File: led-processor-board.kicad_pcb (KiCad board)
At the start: 2 copper layers, 100 x 89.5 mm, 127 parts, among them J1 USB-C, J2 SPARE, J3 SWD, J4 12V IN, J5 OUT1, J6 OUT2, J7 OUT3, J8 OUT4, SW1 434133025816, SW2 434133025816, U1 RP2350B, U2 NCP1117ST33T3G, U3 W25Q128JVSIQ, U4 APS6404L-3SQR-SN, U5 RM2, U6 DS3231SN, U7 TPS54202H, X1 12MHz

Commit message: Move the PSRAM to the top side for one-sided JLCPCB assembly
U4 (APS6404L) and its C22, R11 and R13 were under the flash on the bottom,
as on Pi's board. They now sit on top just left of the flash, with the
QSPI branches run from Pi's vias under U3, so every part is on the top.
DRC: nothing unconnected, no copper errors.

Co-Authored-By: Claude Opus 5.5 (1M context) <noreply@anthropic.com>
Claude-Session: https://claude.ai/code/session_01CYnkeL97vxsPSCyXSKGro9
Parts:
- C22, R11, R13, U4: moved to F.Cu
- moved R11 20.5 mm to (73.0, 77.4), turned to 0 degrees
- moved R13 19.6 mm to (73.0, 75.2)
- moved U4 16.3 mm to (79.5, 78.0), turned to 0 degrees
- moved C22 10.2 mm to (83.0, 73.6), turned to 0 degrees
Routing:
- net /GPIO47_ADC7: track 36.1 -> 60.2 mm, vias 1 -> 2
- net /QSPI_SD3: track 17.0 -> 40.0 mm, vias 1 -> 3
- net /QSPI_SD2: track 18.3 -> 38.4 mm, vias 1 -> 2
- net +3V3: track 235.0 -> 249.5 mm, vias 14 -> 15
- net /QSPI_SD0: track 13.8 -> 26.9 mm, vias 1 -> 2
- net /QSPI_SCLK: track 15.5 -> 28.3 mm, vias 1 -> 2
- net /QSPI_SD1: track 23.4 -> 35.9 mm, vias 1 -> 2
- net /PSRAM_CS: track 7.27 -> 6.23 mm
- net GND: track 58.3 -> 59.3 mm, vias 143 -> 141

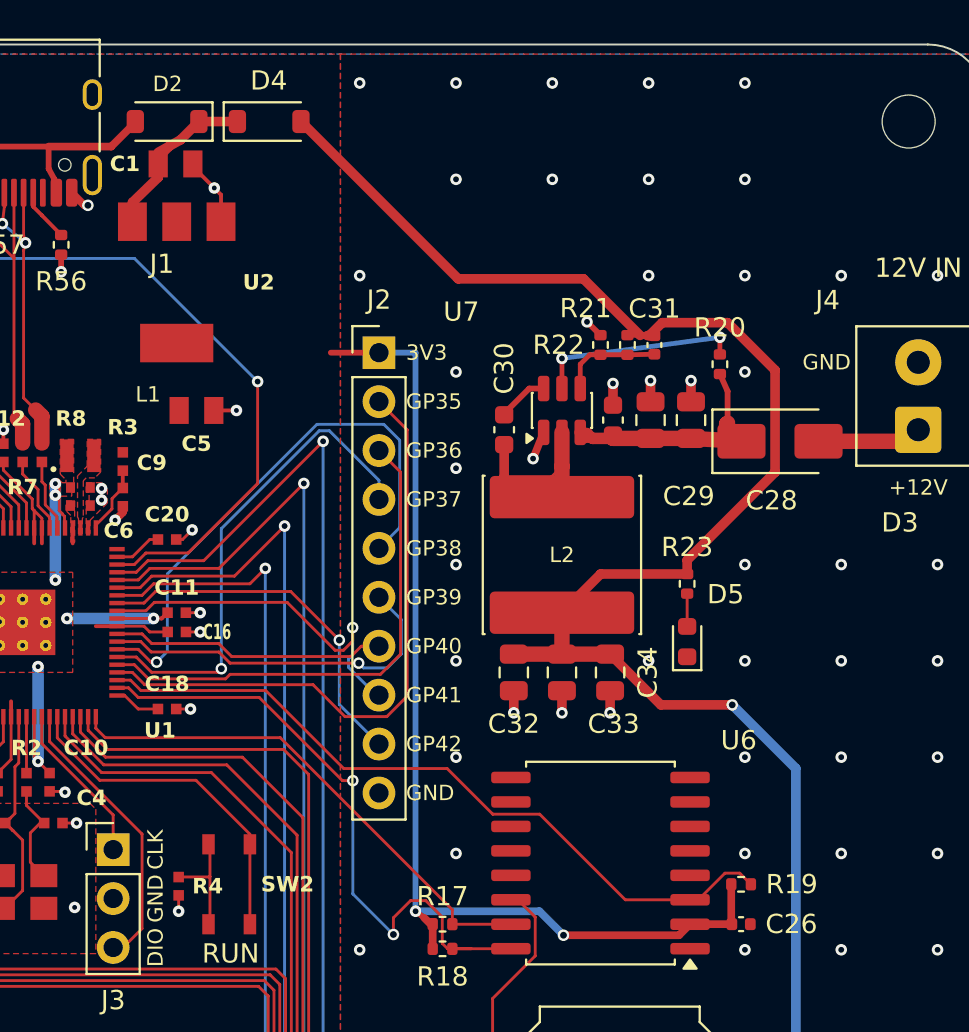
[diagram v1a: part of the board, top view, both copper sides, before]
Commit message: Move the spare GPIO header (J2) to the top edge
J2 now sits along the top edge right of the USB-C, so wires leave from
the board edge. GPIO35-42 are hand-routed: top-layer escapes from the
core, a via row left of the buck, then a bottom-layer fan-out to the
pins, with the ADC lanes (GPIO40-42) furthest from the switch node.
The +3V3 hop from the core pour to the RTC moves below the via row.
post.py keeps stitching vias off silkscreen text.

Co-Authored-By: Claude Opus 5.5 (1M context) <noreply@anthropic.com>
Claude-Session: https://claude.ai/code/session_01CYnkeL97vxsPSCyXSKGro9
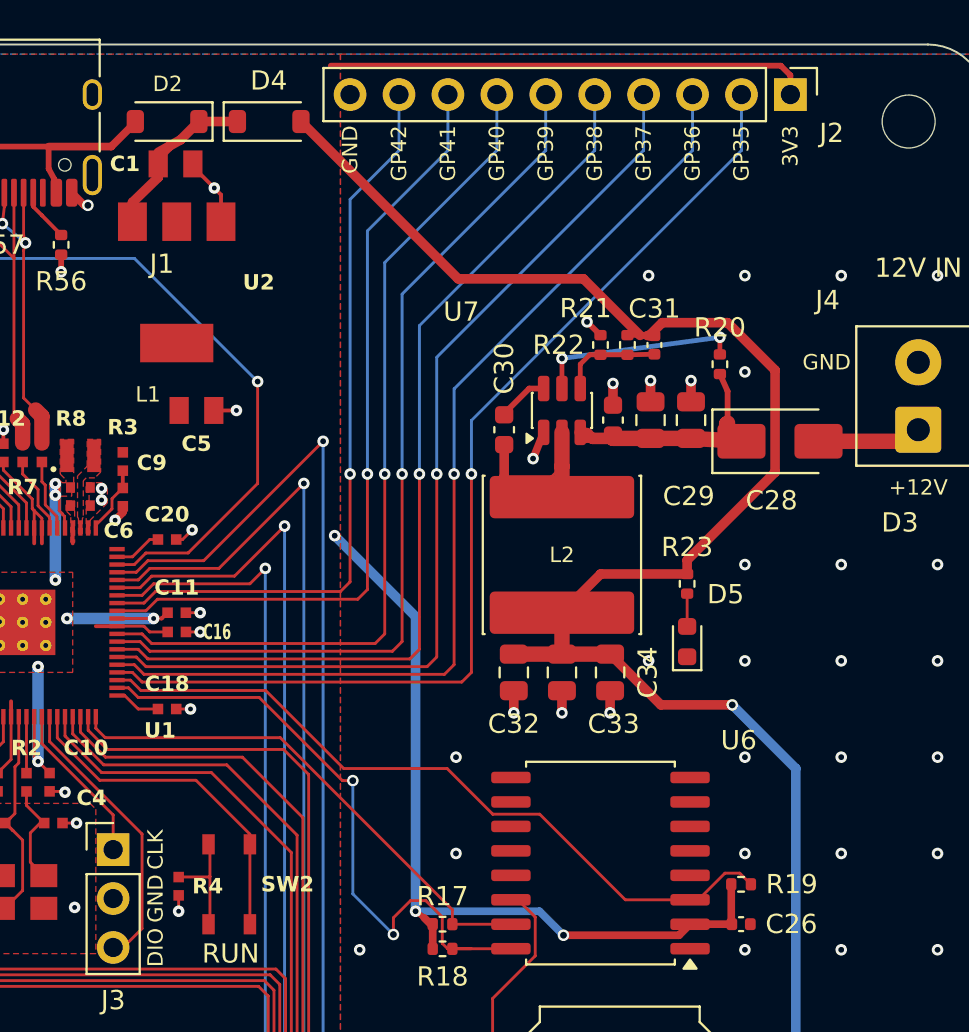
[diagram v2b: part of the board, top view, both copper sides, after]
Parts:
- moved J2 25.2 mm to (139.9, 72.6), turned to -90 degrees
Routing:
- net /GPIO40_ADC0: track 14.3 -> 44.7 mm, vias 0 -> 1
- net /GPIO39: track 19.1 -> 46.7 mm
- net /GPIO36: track 26.6 -> 52.6 mm, vias 0 -> 1
- net /GPIO37: track 25.4 -> 50.7 mm
- net /GPIO35: track 32.4 -> 54.6 mm, vias 0 -> 1
- net /GPIO41_ADC1: track 18.7 -> 40.9 mm
- net /GPIO38: track 28.8 -> 48.7 mm
- net /GPIO42_ADC2: track 19.1 -> 38.9 mm
- net +3V3: track 249.5 -> 262.4 mm, vias 15 -> 16
- net GND: vias 141 -> 127

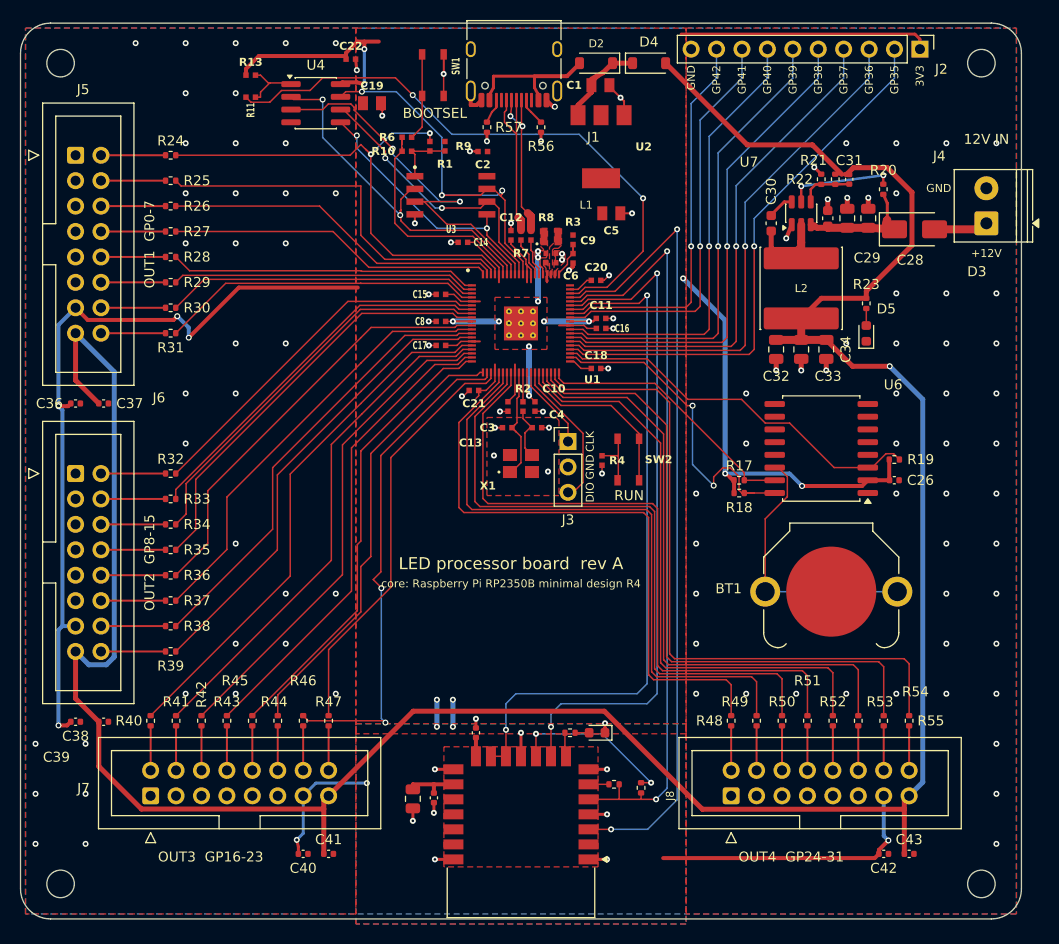
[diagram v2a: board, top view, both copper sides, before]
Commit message: Bottom shrouds to the edge; add J9 for the RM2's spare GPIOs
J7/J8 move down until their bottom pins sit just above the antenna
strip, like the left-edge shrouds; J8 also shifts 1.6 mm left to clear
the corner hole. Their 3V3/5V runs are hand-routed through the channel
between the pin rows (one net per layer) and the caps sit above the
shrouds' right ends. This replaces the old OUT4 3V3 run along the
bottom edge into the radio's 3V3 pour.

J9 (1x3: WL_GPIO1, WL_GPIO2, GND) breaks out the CYW43's two unused
GPIOs beside the RM2, in the schematic and on the board; C23/C24 move
up to make room. DRC with schematic parity is clean apart from the
inherited warnings.

Co-Authored-By: Claude Opus 5.5 (1M context) <noreply@anthropic.com>
Claude-Session: https://claude.ai/code/session_01CYnkeL97vxsPSCyXSKGro9
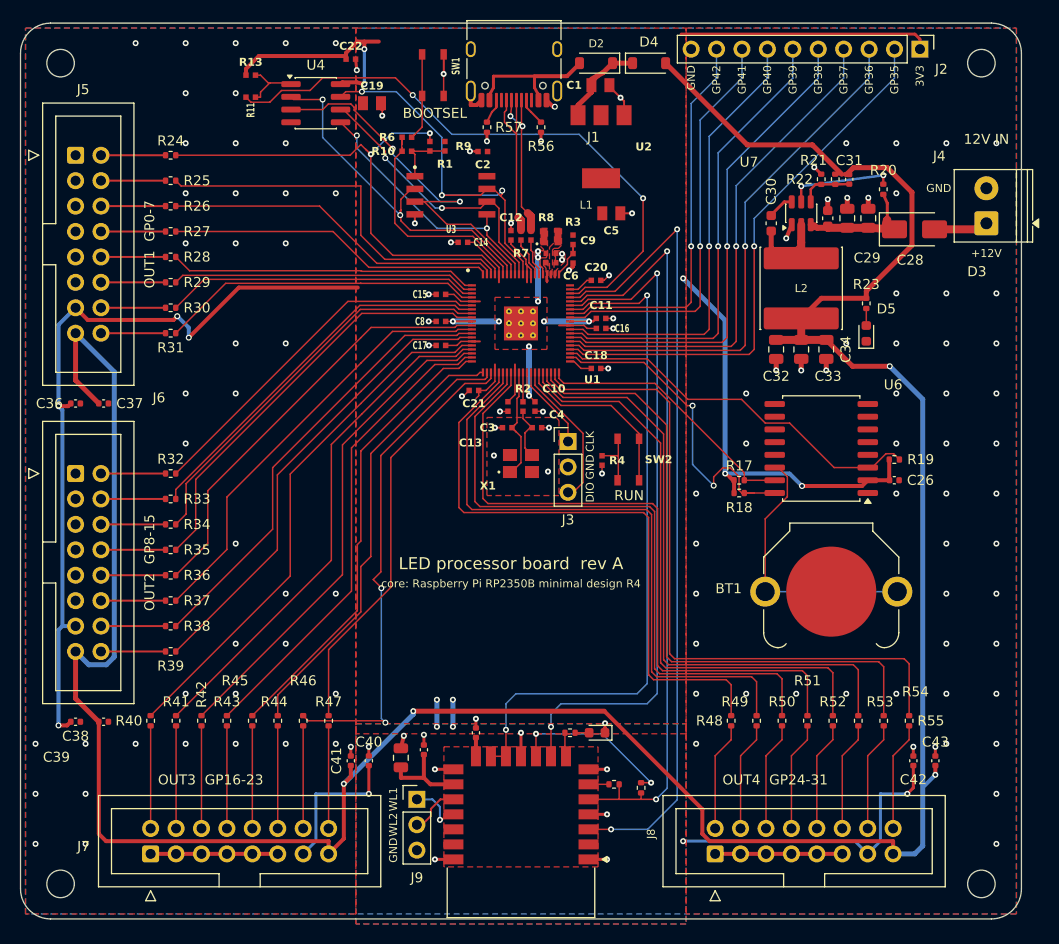
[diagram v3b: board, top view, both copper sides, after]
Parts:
- added J9: WL_GPIO, Connector_PinHeader_2.54mm:PinHeader_1x03_P2.54mm_Vertical, F.Cu at (89.6, 147.6)
- moved C40 11.4 mm to (84.8, 143.7), turned to 90 degrees
- moved C42 9.76 mm to (139.2, 143.7), turned to 90 degrees
- moved C43 9.66 mm to (141.4, 143.7), turned to 90 degrees
- moved C41 9.56 mm to (83.0, 143.7), turned to 90 degrees
- moved J8 6.02 mm to (119.4, 153.0)
- moved J7 5.80 mm to (63.0, 153.0)
- moved C24 4.90 mm to (90.3, 142.6), turned to 90 degrees
- moved C23 4.27 mm to (88.0, 143.4), turned to 90 degrees
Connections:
- U5 pad 17: unconnected-(U5-GPIO2-Pad17) -> /WL_GPIO2
- U5 pad 18: unconnected-(U5-GPIO1-Pad18) -> /WL_GPIO1
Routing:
- net GND: track 59.3 -> 88.4 mm, vias 127 -> 138
- net +5V: track 271.2 -> 287.5 mm, vias 1 -> 4
- net +3V3: track 262.4 -> 270.7 mm
- net Net-(J8-Pin_8): track 4.45 -> 10.9 mm
- net Net-(J8-Pin_6): track 4.45 -> 10.9 mm
- net Net-(J8-Pin_2): track 4.45 -> 10.9 mm
- net Net-(J8-Pin_16): track 4.45 -> 10.9 mm
- net Net-(J8-Pin_10): track 4.45 -> 10.9 mm
- net Net-(J8-Pin_14): track 4.45 -> 10.9 mm
- net Net-(J8-Pin_4): track 4.45 -> 10.9 mm
- net Net-(J8-Pin_12): track 4.45 -> 10.9 mm
- net Net-(J7-Pin_8): track 4.45 -> 10.2 mm
- net Net-(J7-Pin_6): track 4.45 -> 10.2 mm
- net Net-(J7-Pin_4): track 4.45 -> 10.2 mm
- net Net-(J7-Pin_2): track 4.45 -> 10.2 mm
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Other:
- board text added: "WL1"
- board text added: "WL2"

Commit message: Move J9 and the SWD header (J3) under the board name
Both 1x3 headers now sit side by side in the open area under the board
name, J9 (WL_GPIO1, WL_GPIO2, GND) on the left and J3 (SWCLK, GND, SWD)
on the right, with pin labels under each. C23/C24 go back to Pi's
spots beside the RM2. SWCLK/SWD keep their escapes from the core and
hop under the GPIO24-27 run on the bottom layer; WL_GPIO1/2 run up on
the bottom layer. DRC with schematic parity is unchanged.

Co-Authored-By: Claude Opus 5.5 (1M context) <noreply@anthropic.com>
Claude-Session: https://claude.ai/code/session_01CYnkeL97vxsPSCyXSKGro9
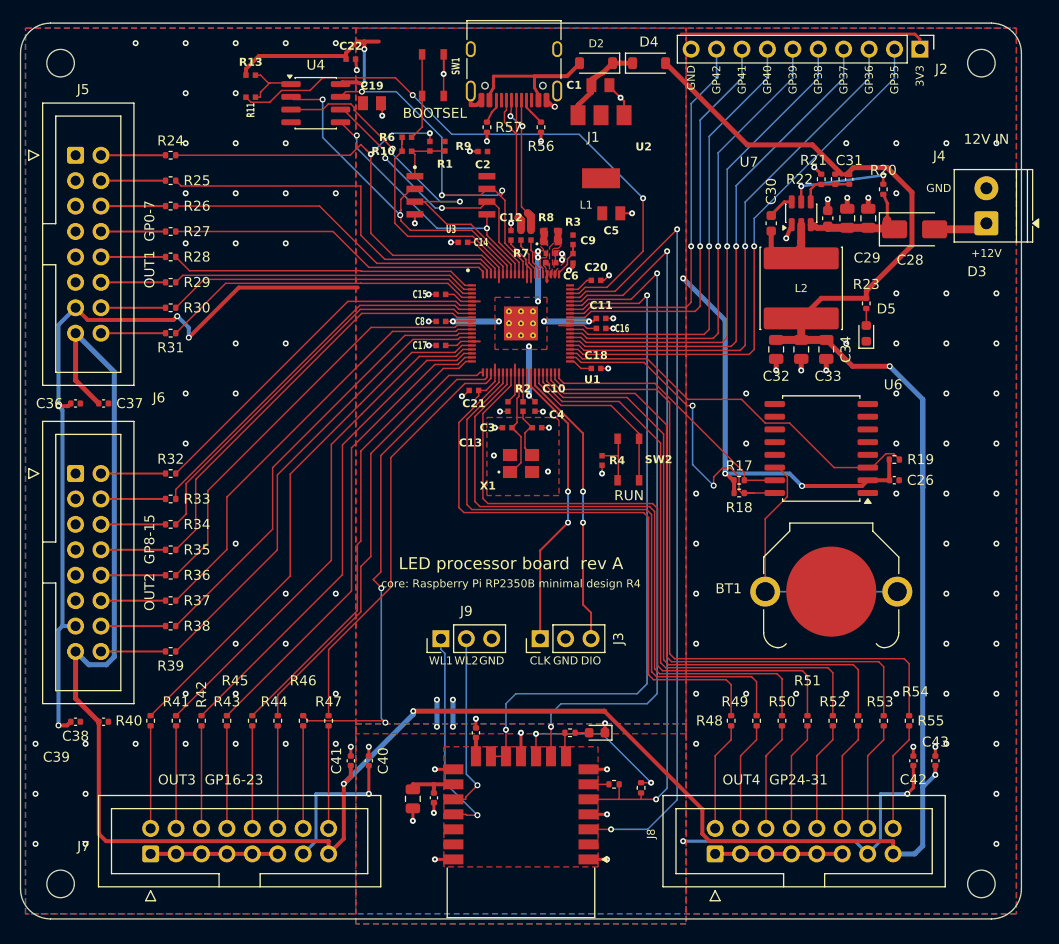
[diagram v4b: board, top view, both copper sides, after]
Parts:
- moved J3 19.9 mm to (101.9, 131.5), turned to 90 degrees
- moved J9 16.2 mm to (92.0, 131.5), turned to 90 degrees
- moved C24 4.90 mm to (91.3, 147.4), turned to -90 degrees
- moved C23 4.27 mm to (89.2, 147.5), turned to -90 degrees
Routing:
- net /SWCLK: track 8.43 -> 29.3 mm, vias 0 -> 2
- net /WL_GPIO1: track 5.37 -> 21.6 mm
- net /SWD: track 14.9 -> 28.9 mm, vias 0 -> 2
- net /WL_GPIO2: track 5.11 -> 18.2 mm, vias 0 -> 1
- net +5V: track 287.5 -> 296.3 mm
- net +3V3: track 270.7 -> 267.2 mm

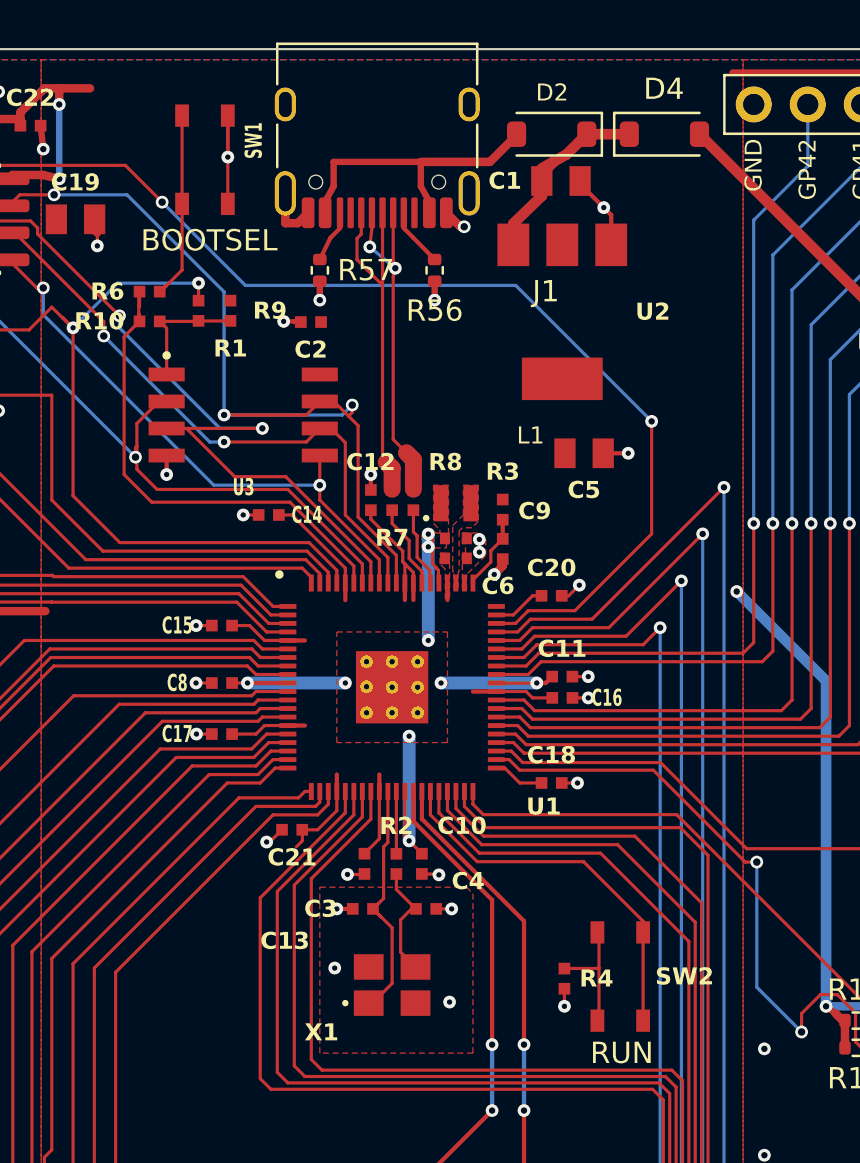
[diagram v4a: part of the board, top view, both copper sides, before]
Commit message: LCSC buttons, and JLCPCB files for SMD-only assembly
SW1/SW2 become the XKB TS-1088R-02526 (LCSC C455281) in Pi's spots, with
the schematic symbols swapped to Switch:SW_Push. tools/jlc.py writes fab/:
gerbers + drill zip, and a BOM and CPL with only the SMD parts JLC places.
The RM2, battery holder, headers, shrouds and J4 are left to hand-solder.

Co-Authored-By: Claude Opus 5.5 (1M context) <noreply@anthropic.com>
Claude-Session: https://claude.ai/code/session_01CYnkeL97vxsPSCyXSKGro9
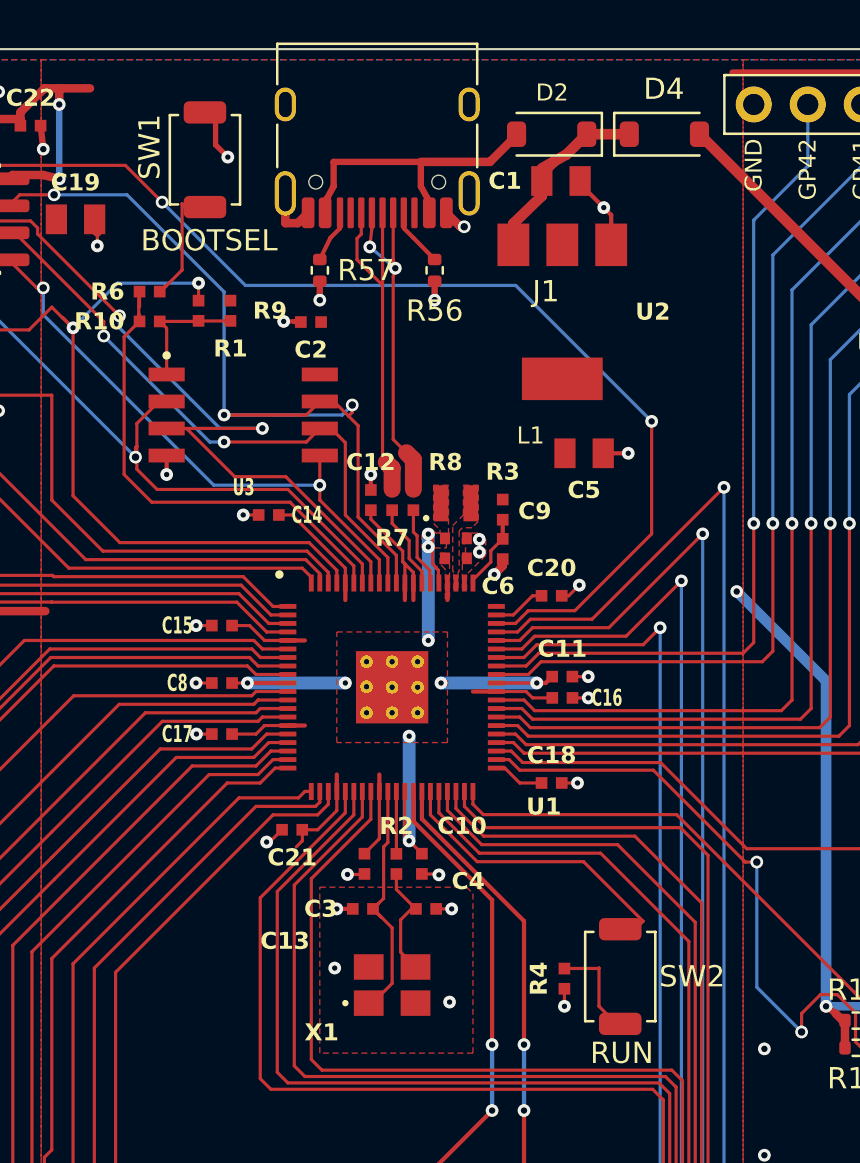
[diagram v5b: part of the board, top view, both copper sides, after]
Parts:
- SW1, SW2: value 434133025816 -> TS-1088R-02526; footprint RPI_COMPILED:wurthelek_434133025816 -> Button_Switch_SMD:SW_SPST_TS-1088-xR025
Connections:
- SW1 pad 2: GND -> /~{USB_BOOT}
- SW2 pad 2: Net-(R4-Pad1) -> /RUN
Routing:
- net /RUN: track 17.9 -> 13.7 mm
- net GND: track 88.3 -> 84.5 mm
- net /~{USB_BOOT}: track 9.09 -> 6.08 mm
- net Net-(R4-Pad1): track 5.94 -> 4.11 mm
